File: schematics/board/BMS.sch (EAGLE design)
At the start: 11 parts

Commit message: Новые схемы
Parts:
- renumbered DS18B20_1 to DS18B20B, DS18B20_2 to DS18B20A, DS18B20_3 to DS18B20, DS18B20_4 to DS18B20C
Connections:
- removed net B-5: B+.P$1, VAR5.3
- removed net GND: B-.P$1, DS18B20.1, DS18B20A.1, DS18B20B.1, DS18B20C.1, VAR5.1
- new net N$1: DS18B20.1, DS18B20A.1, DS18B20B.1, DS18B20C.1, VAR5.4
- new net N$2: B-.P$1, VAR5.6
- net 1W: now also VAR5.3; no longer VAR5.5
- net BMS+: now also B+.P$1, VAR5.8; no longer VAR5.6
- net N$205: now also VAR5.7; no longer VAR5.2
- net N$206: now also VAR5.2; no longer VAR5.7
- net N$3: now also VAR5.1; no longer VAR5.8
- net VDD: now also VAR5.5; no longer VAR5.4
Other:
- moved on the sheet: VAR5

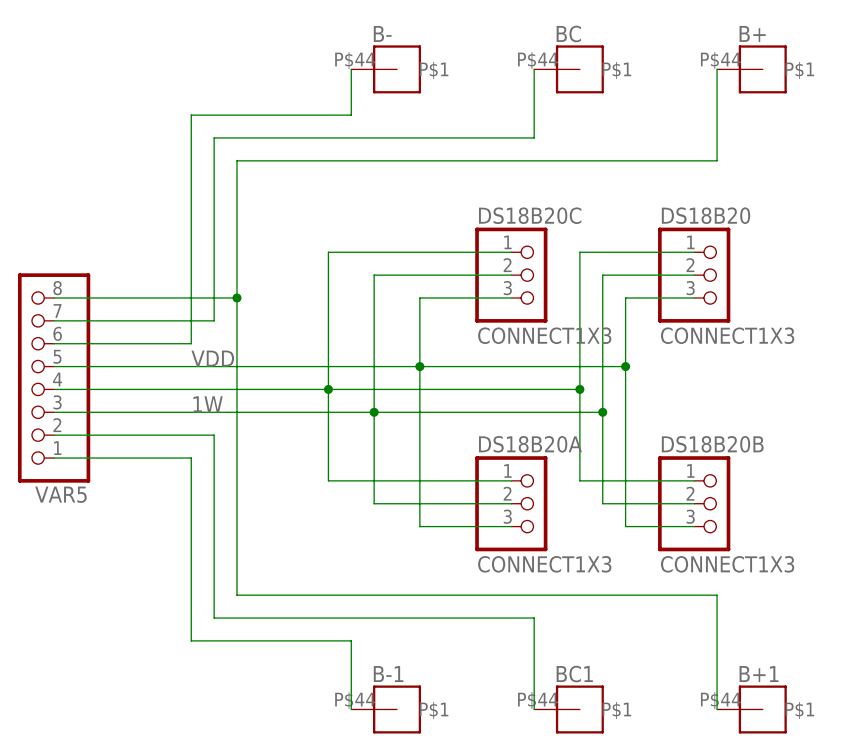
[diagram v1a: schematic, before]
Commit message: Исправлены ошибки в плате АБ
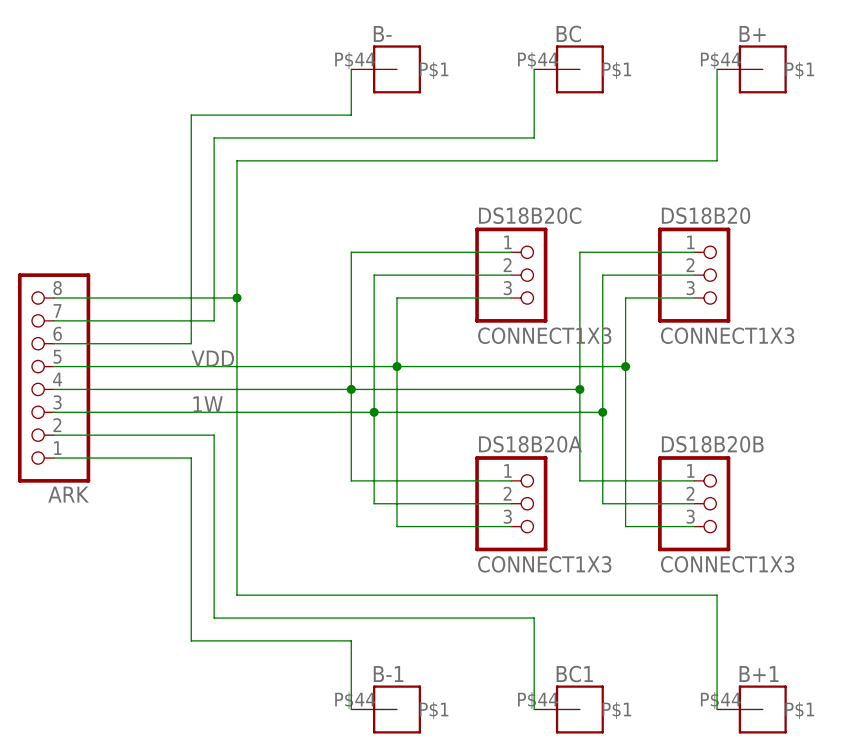
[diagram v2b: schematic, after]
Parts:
- renumbered VAR5 to ARK
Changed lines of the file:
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@@
 <part name="BC1" library="CanCubeSat" deviceset="DRILLBAT5" device=""/>
 <part name="B-1" library="CanCubeSat" deviceset="DRILLBAT5" device=""/>
-<part name="VAR5" library="pinheadCS" deviceset="PINHD-1X8" device=""/>
+<part name="ARK" library="pinheadCS" deviceset="PINHD-1X8" device=""/>
 </parts>
 <sheets>
@@
 <attribute name="NAME" x="101.346" y="140.208" size="1.778" layer="95"/>
 </instance>
-<instance part="VAR5" gate="A" x="63.5" y="175.26" smashed="yes" rot="R180">
+<instance part="ARK" gate="A" x="63.5" y="175.26" smashed="yes" rot="R180">
 <attribute name="NAME" x="69.85" y="161.925" size="1.778" layer="95" rot="R180"/>
 <attribute name="VALUE" x="69.85" y="187.96" size="1.778" layer="96" rot="R180"/>
@@
 <pinref part="DS18B20A" gate="G$1" pin="2"/>
 <pinref part="DS18B20B" gate="G$1" pin="2"/>
-<pinref part="VAR5" gate="A" pin="3"/>
+<pinref part="ARK" gate="A" pin="3"/>
 <wire x1="66.04" y1="170.18" x2="101.6" y2="170.18" width="0.1524" layer="91"/>
 </segment>
@@
 <net name="VDD" class="0">
 <segment>
-<wire x1="106.68" y1="175.26" x2="106.68" y2="182.88" width="0.1524" layer="91"/>
-<wire x1="106.68" y1="182.88" x2="116.84" y2="182.88" width="0.1524" layer="91"/>
-<junction x="106.68" y="175.26"/>
-<wire x1="129.54" y1="175.26" x2="106.68" y2="175.26" width="0.1524" layer="91"/>
+<wire x1="104.14" y1="175.26" x2="104.14" y2="182.88" width="0.1524" layer="91"/>
+<wire x1="104.14" y1="182.88" x2="116.84" y2="182.88" width="0.1524" layer="91"/>
+<junction x="104.14" y="175.26"/>
+<wire x1="129.54" y1="175.26" x2="104.14" y2="175.26" width="0.1524" layer="91"/>
 <wire x1="137.16" y1="157.48" x2="129.54" y2="157.48" width="0.1524" layer="91"/>
 <wire x1="129.54" y1="157.48" x2="129.54" y2="175.26" width="0.1524" layer="91"/>
-<wire x1="116.84" y1="157.48" x2="106.68" y2="157.48" width="0.1524" layer="91"/>
-<wire x1="106.68" y1="157.48" x2="106.68" y2="175.26" width="0.1524" layer="91"/>
+<wire x1="116.84" y1="157.48" x2="104.14" y2="157.48" width="0.1524" layer="91"/>
+<wire x1="104.14" y1="157.48" x2="104.14" y2="175.26" width="0.1524" layer="91"/>
 <wire x1="137.16" y1="182.88" x2="129.54" y2="182.88" width="0.1524" layer="91"/>
 <wire x1="129.54" y1="182.88" x2="129.54" y2="175.26" width="0.1524" layer="91"/>
@@
 <pinref part="DS18B20B" gate="G$1" pin="3"/>
 <label x="81.28" y="175.26" size="1.778" layer="95"/>
-<pinref part="VAR5" gate="A" pin="5"/>
-<wire x1="66.04" y1="175.26" x2="106.68" y2="175.26" width="0.1524" layer="91"/>
+<pinref part="ARK" gate="A" pin="5"/>
+<wire x1="66.04" y1="175.26" x2="104.14" y2="175.26" width="0.1524" layer="91"/>
 </segment>
 </net>
@@
 <wire x1="139.7" y1="208.28" x2="139.7" y2="198.12" width="0.1524" layer="91"/>
 <wire x1="139.7" y1="198.12" x2="86.36" y2="198.12" width="0.1524" layer="91"/>
-<pinref part="VAR5" gate="A" pin="8"/>
+<pinref part="ARK" gate="A" pin="8"/>
 <wire x1="86.36" y1="198.12" x2="86.36" y2="182.88" width="0.1524" layer="91"/>
 <wire x1="86.36" y1="182.88" x2="66.04" y2="182.88" width="0.1524" layer="91"/>
@@
 <wire x1="83.82" y1="200.66" x2="83.82" y2="180.34" width="0.1524" layer="91"/>
 <wire x1="83.82" y1="180.34" x2="66.04" y2="180.34" width="0.1524" layer="91"/>
-<pinref part="VAR5" gate="A" pin="7"/>
+<pinref part="ARK" gate="A" pin="7"/>
 </segment>
 </net>
@@
 <wire x1="119.38" y1="147.32" x2="83.82" y2="147.32" width="0.1524" layer="91"/>
 <wire x1="83.82" y1="147.32" x2="83.82" y2="167.64" width="0.1524" layer="91"/>
-<pinref part="VAR5" gate="A" pin="2"/>
+<pinref part="ARK" gate="A" pin="2"/>
 <wire x1="66.04" y1="167.64" x2="83.82" y2="167.64" width="0.1524" layer="91"/>
 </segment>
@@
 <wire x1="99.06" y1="137.16" x2="99.06" y2="144.78" width="0.1524" layer="91"/>
 <wire x1="99.06" y1="144.78" x2="81.28" y2="144.78" width="0.1524" layer="91"/>
-<pinref part="VAR5" gate="A" pin="1"/>
+<pinref part="ARK" gate="A" pin="1"/>
 <wire x1="81.28" y1="144.78" x2="81.28" y2="165.1" width="0.1524" layer="91"/>
 <wire x1="81.28" y1="165.1" x2="66.04" y2="165.1" width="0.1524" layer="91"/>
@@
 <segment>
 <pinref part="DS18B20" gate="G$1" pin="1"/>
-<wire x1="96.52" y1="172.72" x2="124.46" y2="172.72" width="0.1524" layer="91"/>
+<wire x1="99.06" y1="172.72" x2="124.46" y2="172.72" width="0.1524" layer="91"/>
 <wire x1="124.46" y1="172.72" x2="124.46" y2="187.96" width="0.1524" layer="91"/>
 <wire x1="124.46" y1="187.96" x2="137.16" y2="187.96" width="0.1524" layer="91"/>
@@
 <wire x1="124.46" y1="162.56" x2="137.16" y2="162.56" width="0.1524" layer="91"/>
 <pinref part="DS18B20A" gate="G$1" pin="1"/>
-<wire x1="116.84" y1="162.56" x2="96.52" y2="162.56" width="0.1524" layer="91"/>
-<wire x1="96.52" y1="162.56" x2="96.52" y2="172.72" width="0.1524" layer="91"/>
-<junction x="96.52" y="172.72"/>
+<wire x1="116.84" y1="162.56" x2="99.06" y2="162.56" width="0.1524" layer="91"/>
+<wire x1="99.06" y1="162.56" x2="99.06" y2="172.72" width="0.1524" layer="91"/>
+<junction x="99.06" y="172.72"/>
 <pinref part="DS18B20C" gate="G$1" pin="1"/>
-<wire x1="116.84" y1="187.96" x2="96.52" y2="187.96" width="0.1524" layer="91"/>
-<wire x1="96.52" y1="187.96" x2="96.52" y2="172.72" width="0.1524" layer="91"/>
-<pinref part="VAR5" gate="A" pin="4"/>
-<wire x1="66.04" y1="172.72" x2="96.52" y2="172.72" width="0.1524" layer="91"/>
+<wire x1="116.84" y1="187.96" x2="99.06" y2="187.96" width="0.1524" layer="91"/>
+<wire x1="99.06" y1="187.96" x2="99.06" y2="172.72" width="0.1524" layer="91"/>
+<pinref part="ARK" gate="A" pin="4"/>
+<wire x1="66.04" y1="172.72" x2="99.06" y2="172.72" width="0.1524" layer="91"/>
 </segment>
 </net>
@@
 <wire x1="99.06" y1="203.2" x2="81.28" y2="203.2" width="0.1524" layer="91"/>
 <wire x1="81.28" y1="203.2" x2="81.28" y2="177.8" width="0.1524" layer="91"/>
-<pinref part="VAR5" gate="A" pin="6"/>
+<pinref part="ARK" gate="A" pin="6"/>
 <wire x1="81.28" y1="177.8" x2="66.04" y2="177.8" width="0.1524" layer="91"/>
 </segment>
@@
 </sheet>
 </sheets>
+<errors>
+</errors>
 </schematic>
 </drawing>
